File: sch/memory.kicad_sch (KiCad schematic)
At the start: 5 parts

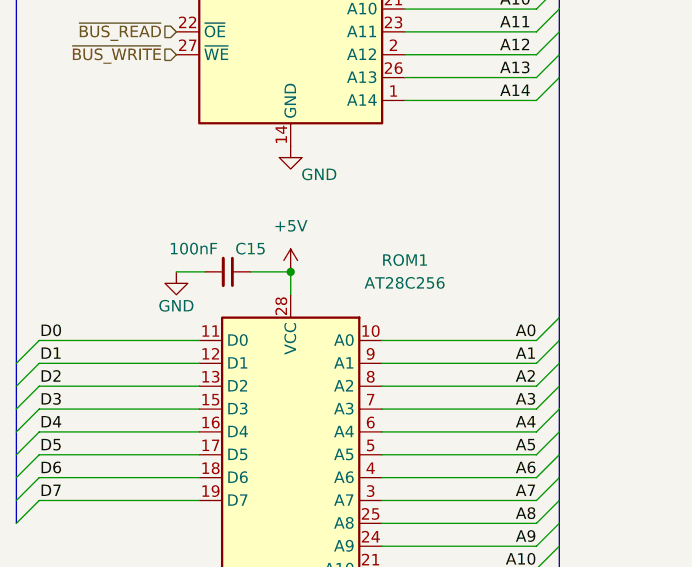
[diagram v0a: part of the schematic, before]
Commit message: Pulldowns, minor reroute
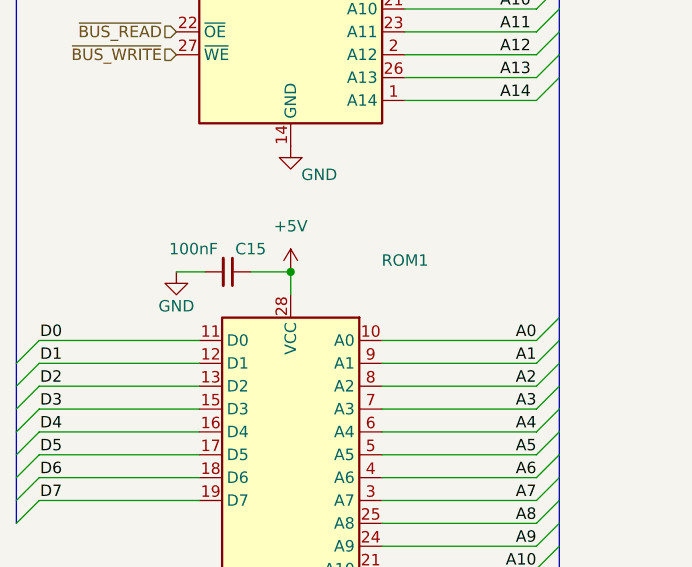
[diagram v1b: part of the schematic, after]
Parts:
- ROM1: value AT28C256 -> (none); footprint Package_DIP:DIP-28_W15.24mm_Socket_LongPads -> (none)
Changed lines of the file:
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@@
     (in_bom yes) (on_board yes)
     (property "Reference" "ROM1" (id 0) (at 128.27 94.615 0))
-    (property "Value" "AT28C256" (id 1) (at 128.27 97.155 0))
-    (property "Footprint" "Package_DIP:DIP-28_W15.24mm_Socket_LongPads" (id 2) (at 115.57 126.365 0)
+    (property "Value" "" (id 1) (at 128.27 97.155 0))
+    (property "Footprint" "" (id 2) (at 115.57 126.365 0)
       (effects (font (size 1.27 1.27)) hide)
     )

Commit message: First completed routing
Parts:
- ROM1: value (none) -> AT28C256; footprint (none) -> Package_DIP:DIP-28_W15.24mm_LongPads
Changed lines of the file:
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@@
     (in_bom yes) (on_board yes)
     (property "Reference" "ROM1" (id 0) (at 128.27 94.615 0))
-    (property "Value" "" (id 1) (at 128.27 97.155 0))
-    (property "Footprint" "" (id 2) (at 115.57 126.365 0)
+    (property "Value" "AT28C256" (id 1) (at 128.27 97.155 0))
+    (property "Footprint" "Package_DIP:DIP-28_W15.24mm_LongPads" (id 2) (at 115.57 126.365 0)
       (effects (font (size 1.27 1.27)) hide)
     )

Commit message: some docs
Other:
- note added: "RAM: 0x0000 - 0x7FFF ROM: 0xB000 - 0xFFFF"
- note added: "System Memory"
- moved on the sheet: C15, C16, R2, RAM1, ROM1

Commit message: serial rollback
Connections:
- net A14: now also RAM1.22 (~{OE}); no longer RAM1.1 (A14)
- net GND: now also RAM1.1 (A14)
- net ~{ROM_CS}: now also ROM1.22 (~{OE})
- removed net ~{BUS_READ}: RAM1.22 (~{OE}), ROM1.22 (~{OE})
- net ~{BUS_WRITE} renamed BUS_R~{W}
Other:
- note added: "RAM: 0x0000 - 0x3FFF ROM: 0x8000 - 0xFFFF"
- note removed: "RAM: 0x0000 - 0x7FFF ROM: 0xB000 - 0xFFFF"
- moved on the sheet: R2
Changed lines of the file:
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@@
     (company "zrthxn")
   )
+  (junction (at 92.075 90.17) (diameter 0) (color 0 0 0 0)
+  )
   (junction (at 92.075 41.91) (diameter 0) (color 0 0 0 0)
   )
+  (junction (at 102.235 156.21) (diameter 0) (color 0 0 0 0)
+  )
   (junction (at 92.075 104.14) (diameter 0) (color 0 0 0 0)
   )
@@
     (stroke (width 0) (type default) (color 0 0 0 0))
   )
-  (bus_entry (at 121.92 82.55) (size -2.54 2.54)
+  (bus_entry (at 121.92 92.71) (size -2.54 2.54)
     (stroke (width 0) (type default) (color 0 0 0 0))
   )
@@
     (stroke (width 0) (type default) (color 0 0 0 0))
   )
+  (wire (pts (xy 102.235 156.21) (xy 102.235 157.48))
+    (stroke (width 0) (type default) (color 0 0 0 0))
+  )
   (wire (pts (xy 79.375 104.14) (xy 82.55 104.14))
     (stroke (width 0) (type default) (color 0 0 0 0))
@@
     (stroke (width 0) (type default) (color 0 0 0 0))
   )
-  (bus (pts (xy 121.92 82.55) (xy 121.92 109.22))
+  (bus (pts (xy 121.92 80.01) (xy 121.92 92.71))
     (stroke (width 0) (type default) (color 0 0 0 0))
   )
@@
     (stroke (width 0) (type default) (color 0 0 0 0))
   )
+  (wire (pts (xy 104.775 85.09) (xy 104.775 90.17))
+    (stroke (width 0) (type default) (color 0 0 0 0))
+  )
   (wire (pts (xy 92.075 106.68) (xy 92.075 104.14))
     (stroke (width 0) (type default) (color 0 0 0 0))
@@
     (stroke (width 0) (type default) (color 0 0 0 0))
   )
+  (wire (pts (xy 111.76 152.4) (xy 121.92 152.4))
+    (stroke (width 0) (type default) (color 0 0 0 0))
+  )
+  (wire (pts (xy 69.215 95.25) (xy 69.215 77.47))
+    (stroke (width 0) (type default) (color 0 0 0 0))
+  )
   (wire (pts (xy 102.235 144.78) (xy 119.38 144.78))
     (stroke (width 0) (type default) (color 0 0 0 0))
@@
     (stroke (width 0) (type default) (color 0 0 0 0))
   )
+  (bus (pts (xy 121.92 92.71) (xy 121.92 109.22))
+    (stroke (width 0) (type default) (color 0 0 0 0))
+  )
   (bus (pts (xy 121.92 49.53) (xy 121.92 52.07))
     (stroke (width 0) (type default) (color 0 0 0 0))
   )
-  (wire (pts (xy 104.775 85.09) (xy 119.38 85.09))
+  (wire (pts (xy 69.215 95.25) (xy 119.38 95.25))
     (stroke (width 0) (type default) (color 0 0 0 0))
   )
@@
     (stroke (width 0) (type default) (color 0 0 0 0))
   )
-  (bus (pts (xy 121.92 80.01) (xy 121.92 82.55))
-    (stroke (width 0) (type default) (color 0 0 0 0))
-  )
   (bus (pts (xy 121.92 46.99) (xy 121.92 49.53))
     (stroke (width 0) (type default) (color 0 0 0 0))
@@
     (stroke (width 0) (type default) (color 0 0 0 0))
   )
+  (wire (pts (xy 104.775 90.17) (xy 92.075 90.17))
+    (stroke (width 0) (type default) (color 0 0 0 0))
+  )
   (wire (pts (xy 102.235 116.84) (xy 119.38 116.84))
     (stroke (width 0) (type default) (color 0 0 0 0))
   )
+  (wire (pts (xy 69.215 77.47) (xy 79.375 77.47))
+    (stroke (width 0) (type default) (color 0 0 0 0))
+  )
   (wire (pts (xy 102.235 147.32) (xy 119.38 147.32))
     (stroke (width 0) (type default) (color 0 0 0 0))
@@
     (stroke (width 0) (type default) (color 0 0 0 0))
   )
-  (wire (pts (xy 102.235 152.4) (xy 128.905 152.4))
+  (wire (pts (xy 102.235 152.4) (xy 104.14 152.4))
     (stroke (width 0) (type default) (color 0 0 0 0))
   )
@@
     (stroke (width 0) (type default) (color 0 0 0 0))
   )
-  (text "RAM: 0x0000 - 0x7FFF\nROM: 0xB000 - 0xFFFF" (at 177.165 158.75 0)
+  (wire (pts (xy 102.235 156.21) (xy 104.14 156.21))
+    (stroke (width 0) (type default) (color 0 0 0 0))
+  )
+  (wire (pts (xy 102.235 154.94) (xy 102.235 156.21))
+    (stroke (width 0) (type default) (color 0 0 0 0))
+  )
+  (text "RAM: 0x0000 - 0x3FFF\nROM: 0x8000 - 0xFFFF" (at 31.75 33.02 0)
     (effects (font (size 1.8 1.8)) (justify left bottom))
   )
@@
     (effects (font (size 1.27 1.27)) (justify right bottom))
   )
-  (label "A14" (at 118.745 85.09 180)
-    (effects (font (size 1.27 1.27)) (justify right bottom))
-  )
-  (hierarchical_label "~{BUS_WRITE}" (shape input) (at 79.375 80.01 180)
-    (effects (font (size 1.27 1.27)) (justify right))
-  )
-  (hierarchical_label "~{BUS_READ}" (shape input) (at 79.375 77.47 180)
+  (label "A14" (at 118.745 95.25 180)
+    (effects (font (size 1.27 1.27)) (justify right bottom))
+  )
+  (hierarchical_label "BUS_R~{W}" (shape input) (at 79.375 80.01 180)
     (effects (font (size 1.27 1.27)) (justify right))
   )
@@
     (effects (font (size 1.27 1.27)) (justify right))
   )
-  (hierarchical_label "~{ROM_CS}" (shape input) (at 102.235 157.48 0)
+  (hierarchical_label "~{ROM_CS}" (shape input) (at 104.14 156.21 0)
     (effects (font (size 1.27 1.27)) (justify left))
   )
-  (hierarchical_label "~{BUS_READ}" (shape input) (at 102.235 154.94 0)
-    (effects (font (size 1.27 1.27)) (justify left))
-  )
-  (symbol (lib_id "power:+5V") (at 128.905 144.78 0) (mirror y) (unit 1)
+  (symbol (lib_id "power:+5V") (at 121.92 152.4 0) (mirror y) (unit 1)
     (in_bom yes) (on_board yes)
-    (property "Reference" "#PWR011" (id 0) (at 128.905 148.59 0)
+    (property "Reference" "#PWR011" (id 0) (at 121.92 156.21 0)
       (effects (font (size 1.27 1.27)) hide)
     )
-    (property "Value" "+5V" (id 1) (at 128.905 140.97 0))
-    (property "Footprint" "" (id 2) (at 128.905 144.78 0)
+    (property "Value" "+5V" (id 1) (at 121.92 148.59 0))
+    (property "Footprint" "" (id 2) (at 121.92 152.4 0)
       (effects (font (size 1.27 1.27)) hide)
     )
-    (property "Datasheet" "" (id 3) (at 128.905 144.78 0)
+    (property "Datasheet" "" (id 3) (at 121.92 152.4 0)
       (effects (font (size 1.27 1.27)) hide)
     )
     (pin "1")
   )
-  (symbol (lib_id "Device:R") (at 128.905 148.59 0) (mirror y) (unit 1)
+  (symbol (lib_id "Device:R") (at 107.95 152.4 270) (mirror x) (unit 1)
     (in_bom yes) (on_board yes)
-    (property "Reference" "R2" (id 0) (at 133.35 147.32 0)
+    (property "Reference" "R2" (id 0) (at 111.125 151.13 90)
       (effects (font (size 1.27 1.27)) (justify left))
     )
-    (property "Value" "10K" (id 1) (at 134.62 149.86 0)
+    (property "Value" "10K" (id 1) (at 114.3 151.13 90)
       (effects (font (size 1.27 1.27)) (justify left))
     )
-    (property "Footprint" "Resistor_SMD:R_0805_2012Metric" (id 2) (at 130.683 148.59 90)
+    (property "Footprint" "Resistor_SMD:R_0805_2012Metric" (id 2) (at 107.95 154.178 90)
       (effects (font (size 1.27 1.27)) hide)
     )
-    (property "Datasheet" "~" (id 3) (at 128.905 148.59 0)
+    (property "Datasheet" "~" (id 3) (at 107.95 152.4 0)
       (effects (font (size 1.27 1.27)) hide)
     )

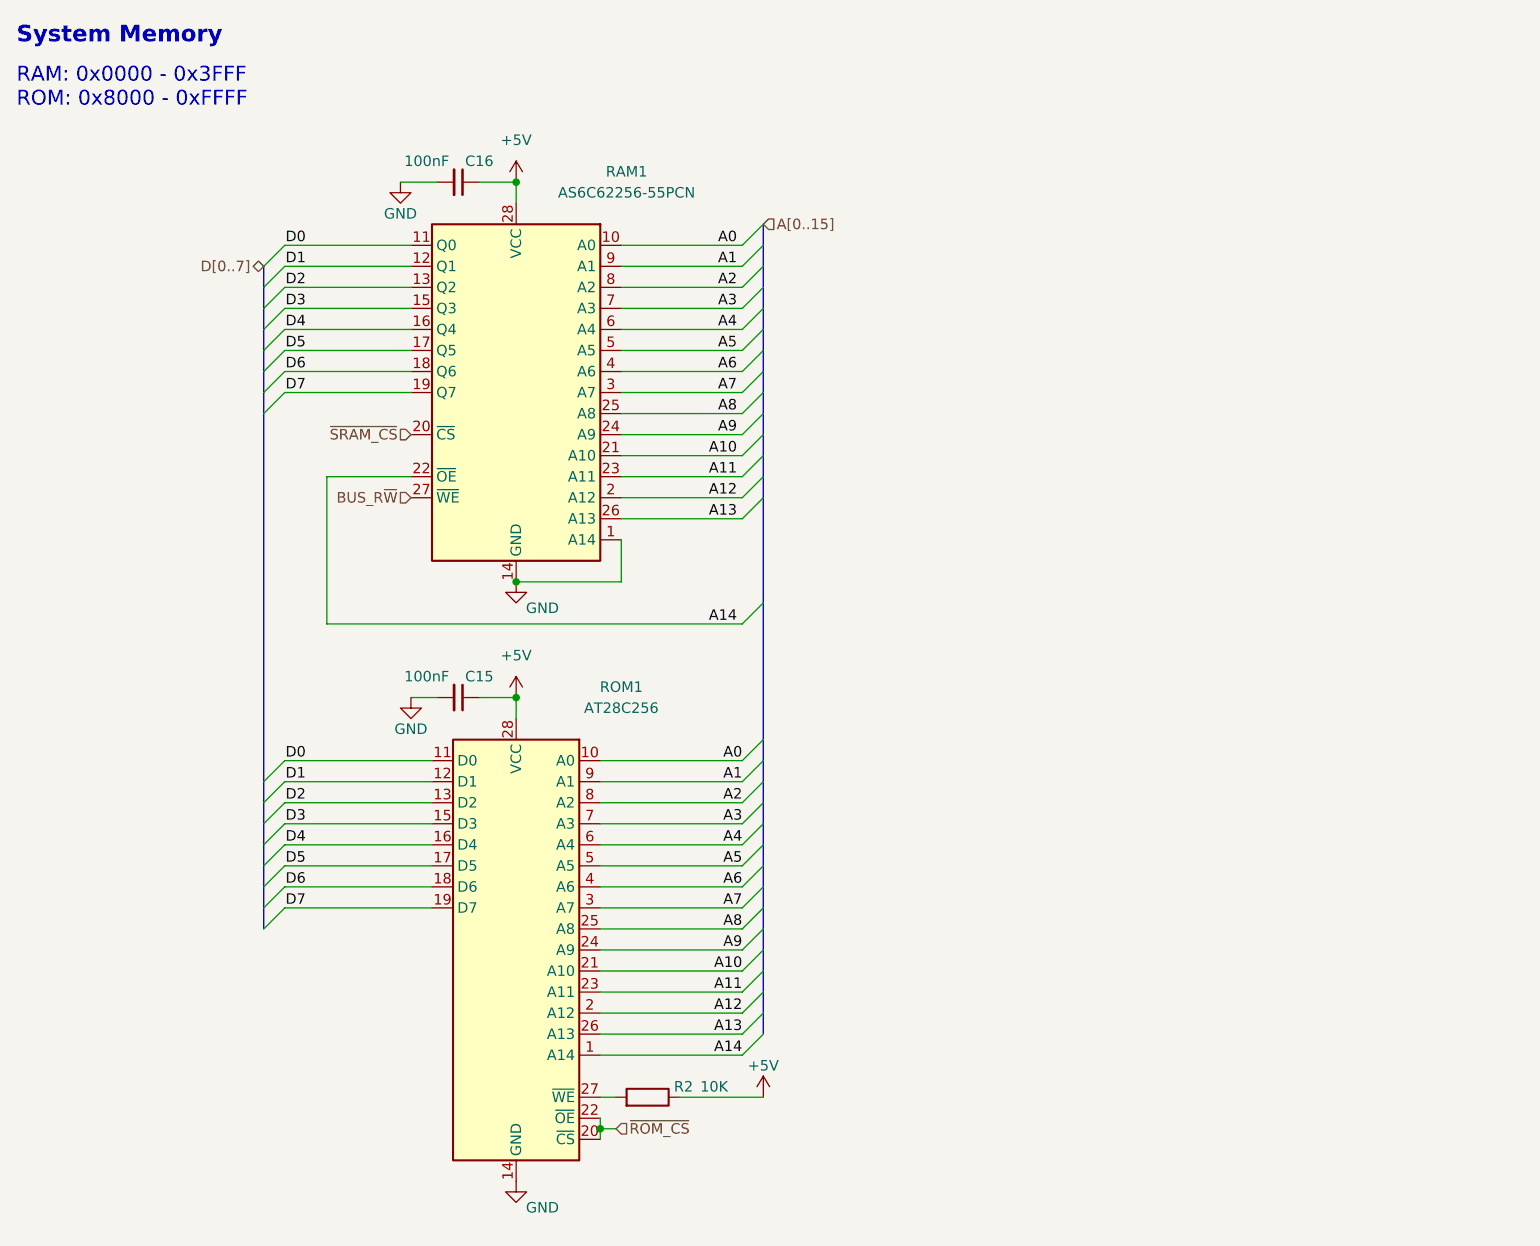
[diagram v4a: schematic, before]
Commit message: fix peripherals, add SPI
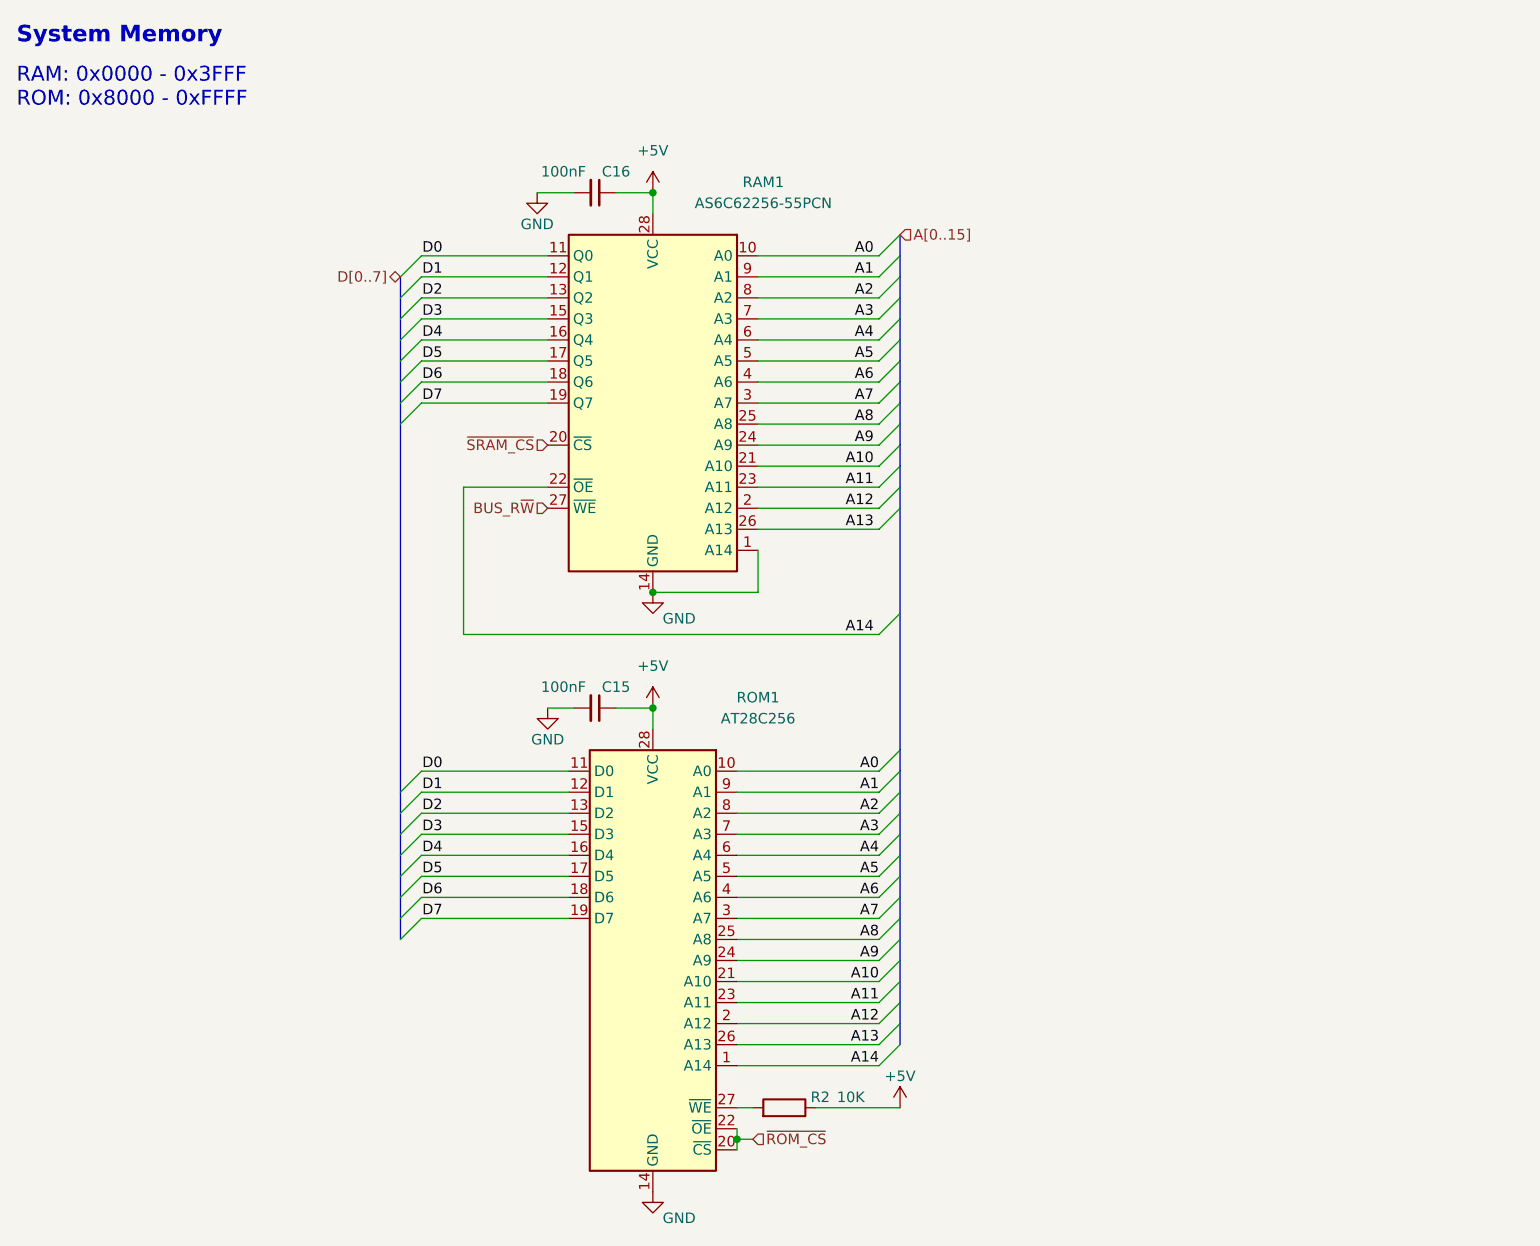
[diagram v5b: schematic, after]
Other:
- moved on the sheet: C15, C16, R2, RAM1, ROM1

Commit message: Cleanup board
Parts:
- R2: value 10K -> (none)
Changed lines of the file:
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@@
   (symbol (lib_id "Device:R") (at 124.46 153.67 270) (mirror x) (unit 1)
     (in_bom yes) (on_board yes)
-    (property "Reference" "R2" (id 0) (at 127.635 152.4 90)
+    (property "Reference" "R2" (id 0) (at 121.285 151.13 90)
       (effects (font (size 1.27 1.27)) (justify left))
     )
-    (property "Value" "10K" (id 1) (at 130.81 152.4 90)
+    (property "Value" "" (id 1) (at 124.46 151.13 90)
       (effects (font (size 1.27 1.27)) (justify left))
     )

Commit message: Clearances
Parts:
- added ROM_WRITE1: Conn_01x03, Connector_PinHeader_2.00mm:PinHeader_1x03_P2.00mm_Vertical, symbol Connector_Generic:Conn_01x03
- R2: value (none) -> 1K
- RAM1: value AS6C62256-55PCN -> AS6C62256-55SINTR; footprint Package_DIP:DIP-28_W15.24mm_LongPads -> Package_SO:SOIC-28W_7.5x17.9mm_P1.27mm
- ROM1: value AT28C256 -> AT28HC256E-90SU; footprint Package_DIP:DIP-28_W15.24mm_LongPads -> Package_SO:SOIC-28W_7.5x17.9mm_P1.27mm
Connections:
- net GND: now also ROM_WRITE1.3 (Pin_3)
- net at R2.2: now also ROM_WRITE1.1 (Pin_1); no longer ROM1.27 (~{WE})
- new net: ROM1.27 (~{WE}), ROM_WRITE1.2 (Pin_2)
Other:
- note added: "Changing jumper to GND will allow writing to ROM from DEBUG header."
- note added: "Tying A14 to ~{OE} and chip's A14 to GND makes the RAM effectively 16K bytes size, with upper half in use."
- moved on the sheet: C15, C16, R2, RAM1, ROM1

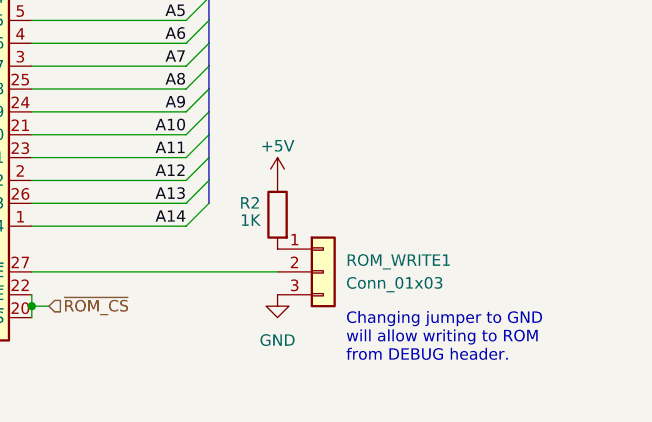
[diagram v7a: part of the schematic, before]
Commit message: bigger header pins
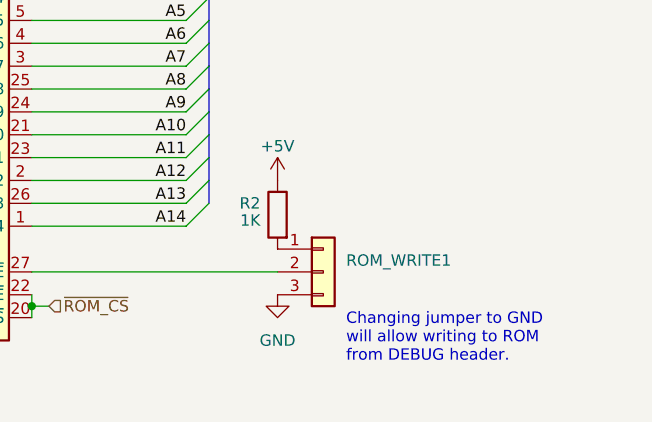
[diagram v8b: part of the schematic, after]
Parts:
- ROM_WRITE1: value Conn_01x03 -> (none); footprint Connector_PinHeader_2.00mm:PinHeader_1x03_P2.00mm_Vertical -> (none)
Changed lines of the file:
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@@
       (effects (font (size 1.27 1.27)) (justify left))
     )
-    (property "Value" "Conn_01x03" (id 1) (at 136.525 154.3049 0)
+    (property "Value" "" (id 1) (at 136.525 154.3049 0)
       (effects (font (size 1.27 1.27)) (justify left))
     )
-    (property "Footprint" "Connector_PinHeader_2.00mm:PinHeader_1x03_P2.00mm_Vertical" (id 2) (at 133.985 153.035 0)
+    (property "Footprint" "" (id 2) (at 133.985 153.035 0)
       (effects (font (size 1.27 1.27)) hide)
     )
